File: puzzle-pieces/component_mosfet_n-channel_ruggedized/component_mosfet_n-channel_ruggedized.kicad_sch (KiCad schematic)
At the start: 15 parts, among them J1 Conn_01x02_Pin, J2 Conn_01x02_Pin, J5 Conn_01x02_Pin, Q1 NDT3055L, Q2 UT3N06G-AB3-R

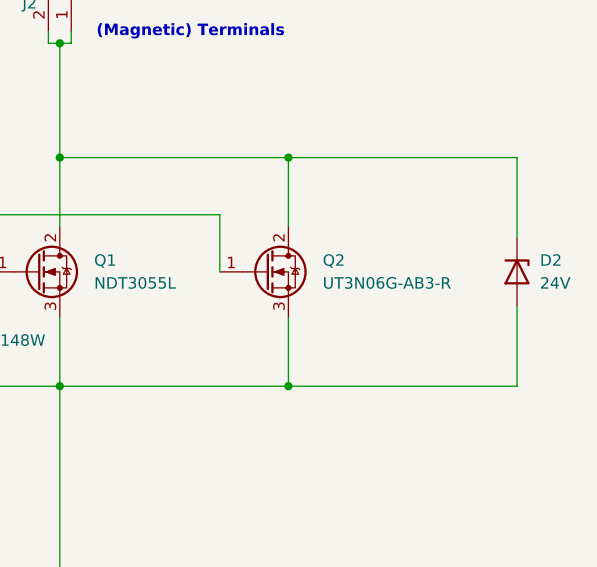
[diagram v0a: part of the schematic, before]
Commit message: Add ruggedized N-channel MOSFET component files
Added README, schematic, PCB, and image files for the ruggedized N-channel MOSFET puzzle piece. Updated PCB value field and removed autosave and lock files.
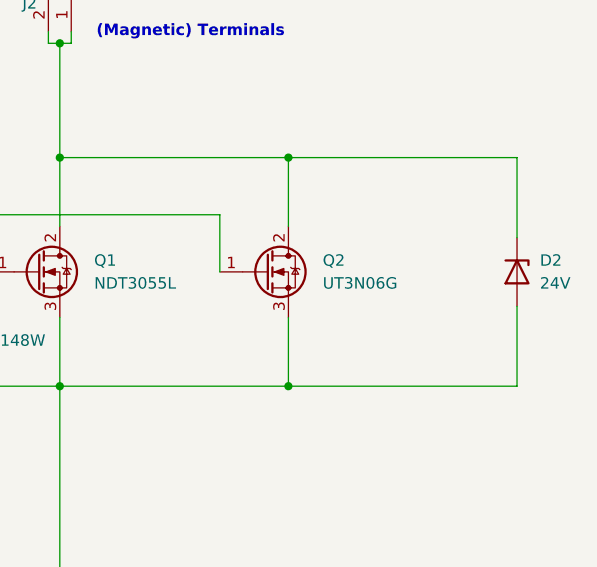
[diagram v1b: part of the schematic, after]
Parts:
- Q2: value UT3N06G-AB3-R -> UT3N06G
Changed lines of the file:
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@@
+	(wire
+		(pts
+			(xy 127 63.5) (xy 152.4 63.5)
+		)
+		(stroke
+			(width 0)
+			(type default)
+		)
+	)
 	(wire
 		(pts
@@
 		(pts
 			(xy 101.6 88.9) (xy 102.87 88.9)
-		)
-		(stroke
-			(width 0)
-			(type default)
-		)
-	)
-	(wire
-		(pts
-			(xy 127 63.5) (xy 152.4 63.5)
 		)
 		(stroke
@@
 			)
 		)
-		(property "Value" "UT3N06G-AB3-R"
+		(property "Value" "UT3N06G"
 			(at 130.81 52.0699 0)
 			(effects
